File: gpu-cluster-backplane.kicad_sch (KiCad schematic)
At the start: 2 parts

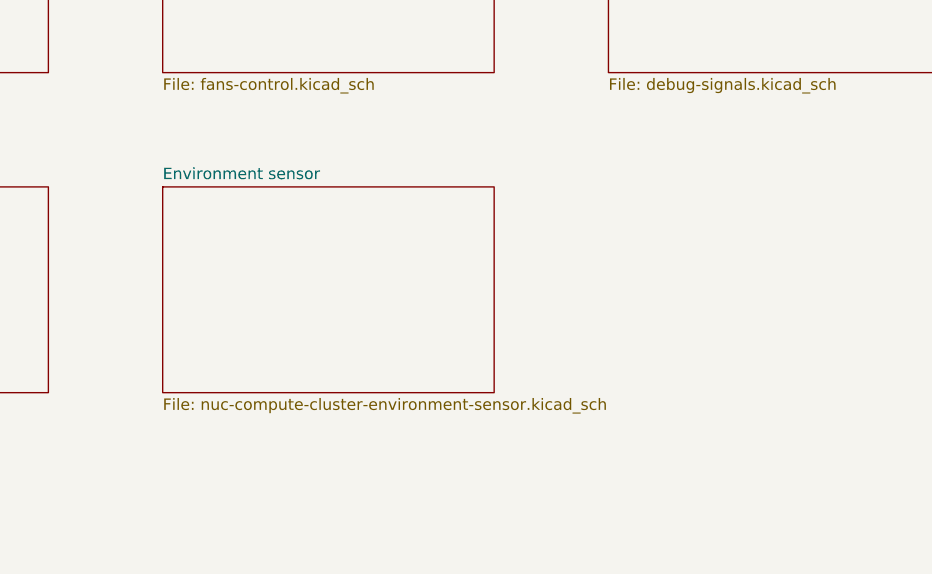
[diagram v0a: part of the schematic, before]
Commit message: Purge enviroment sensor
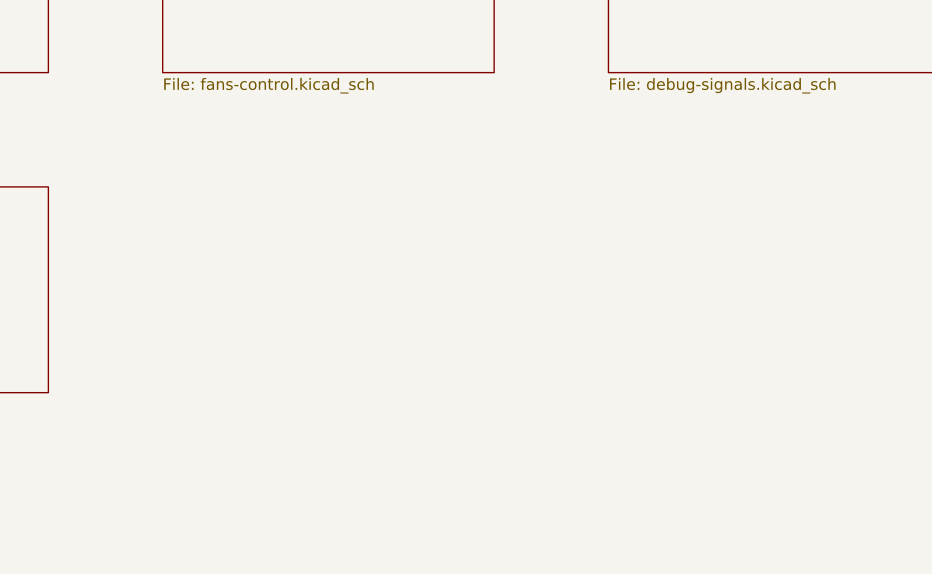
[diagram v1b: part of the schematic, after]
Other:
- removed sheet Environment sensor

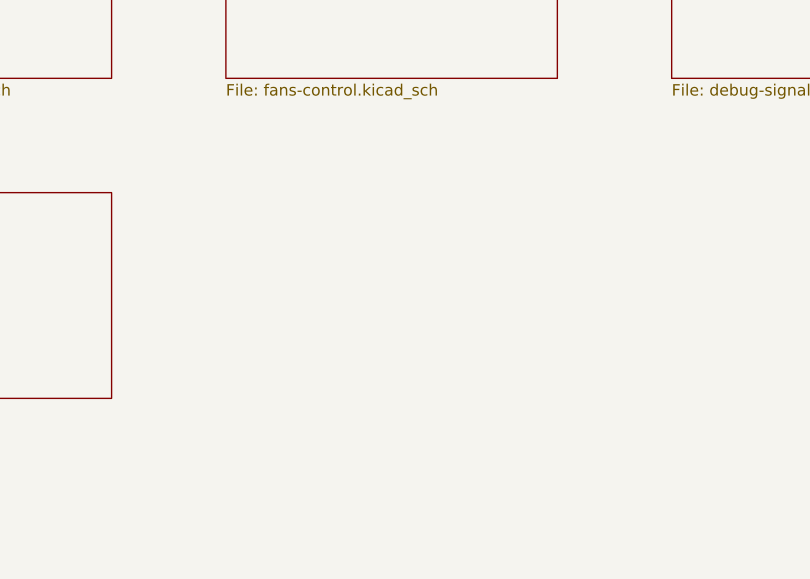
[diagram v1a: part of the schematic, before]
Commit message: Import evnironmental sensor project
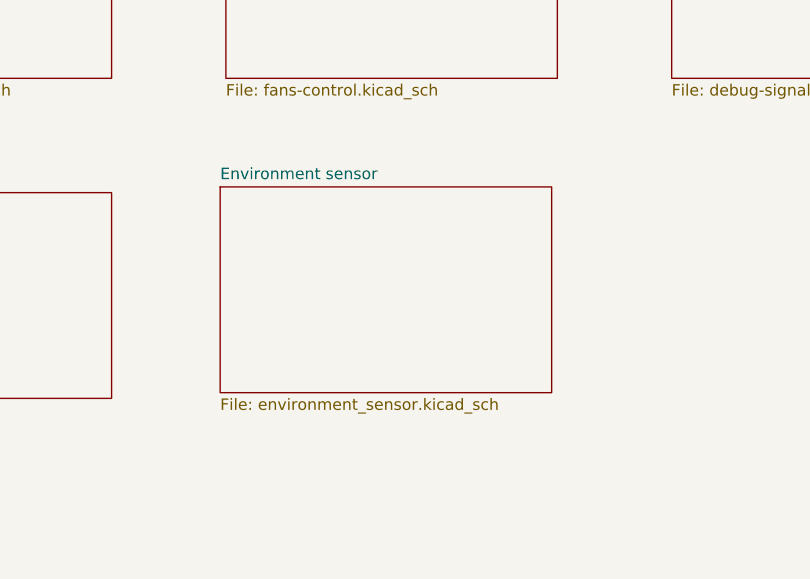
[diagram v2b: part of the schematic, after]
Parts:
- N1: footprint antmicro-footprints:antmicro-logo -> antmicro-footprints:antmicro-logo_scaled_20mm
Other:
- added sheet Environment sensor (environment_sensor.kicad_sch)
